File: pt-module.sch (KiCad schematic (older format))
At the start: 6 parts

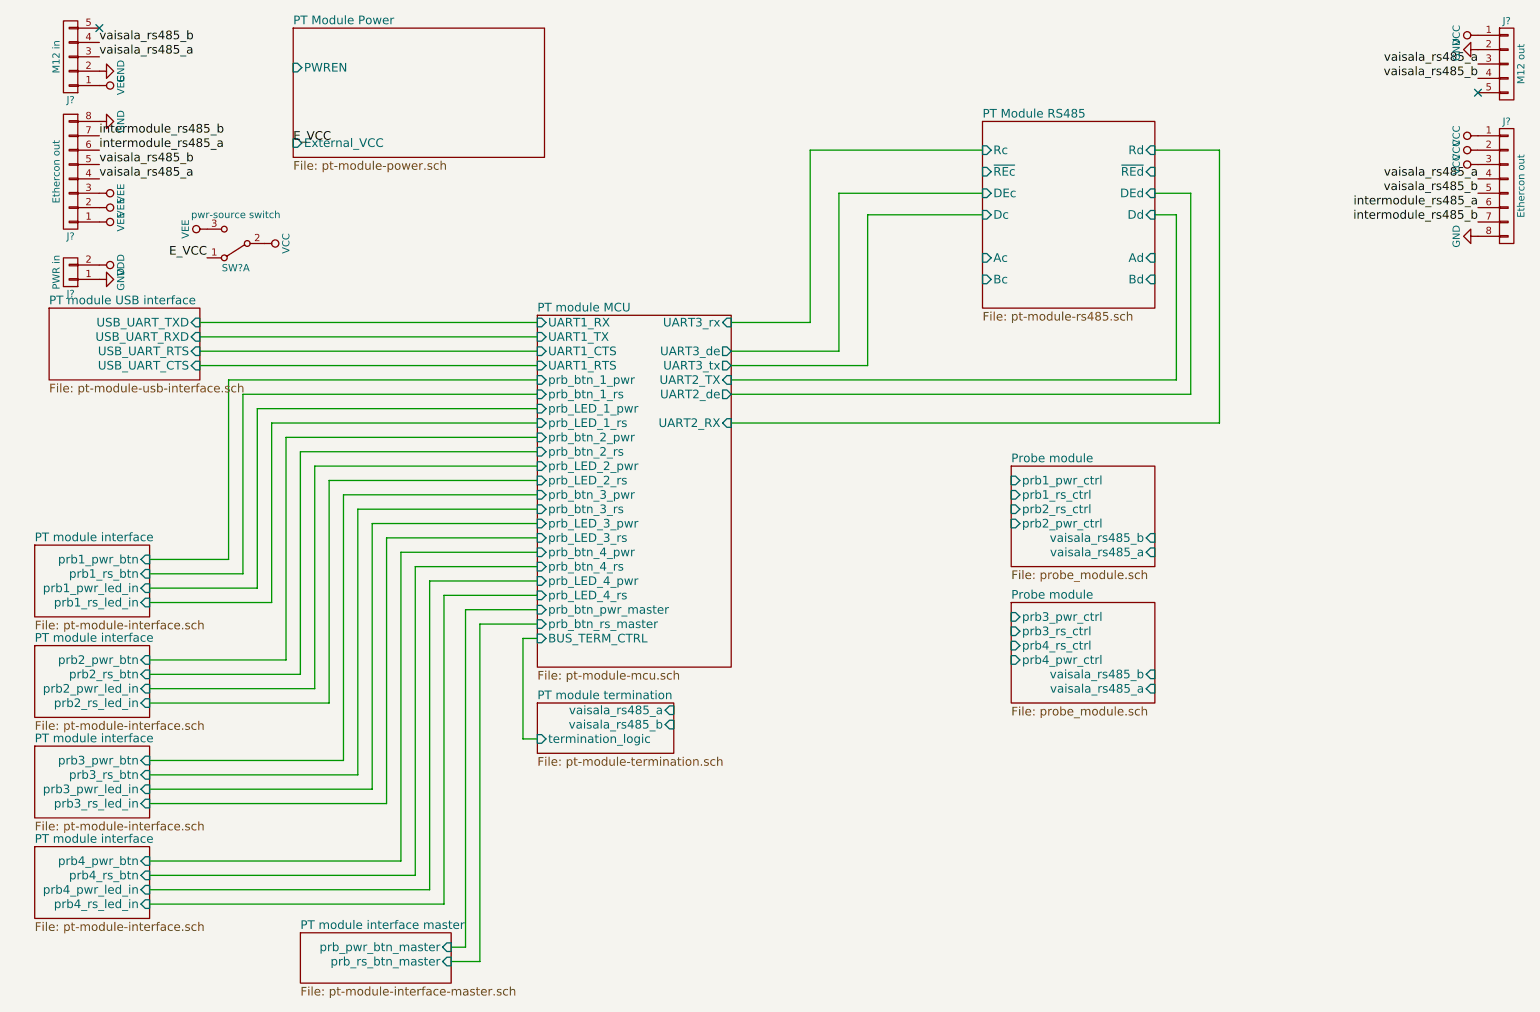
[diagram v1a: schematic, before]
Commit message: Fixed missing components
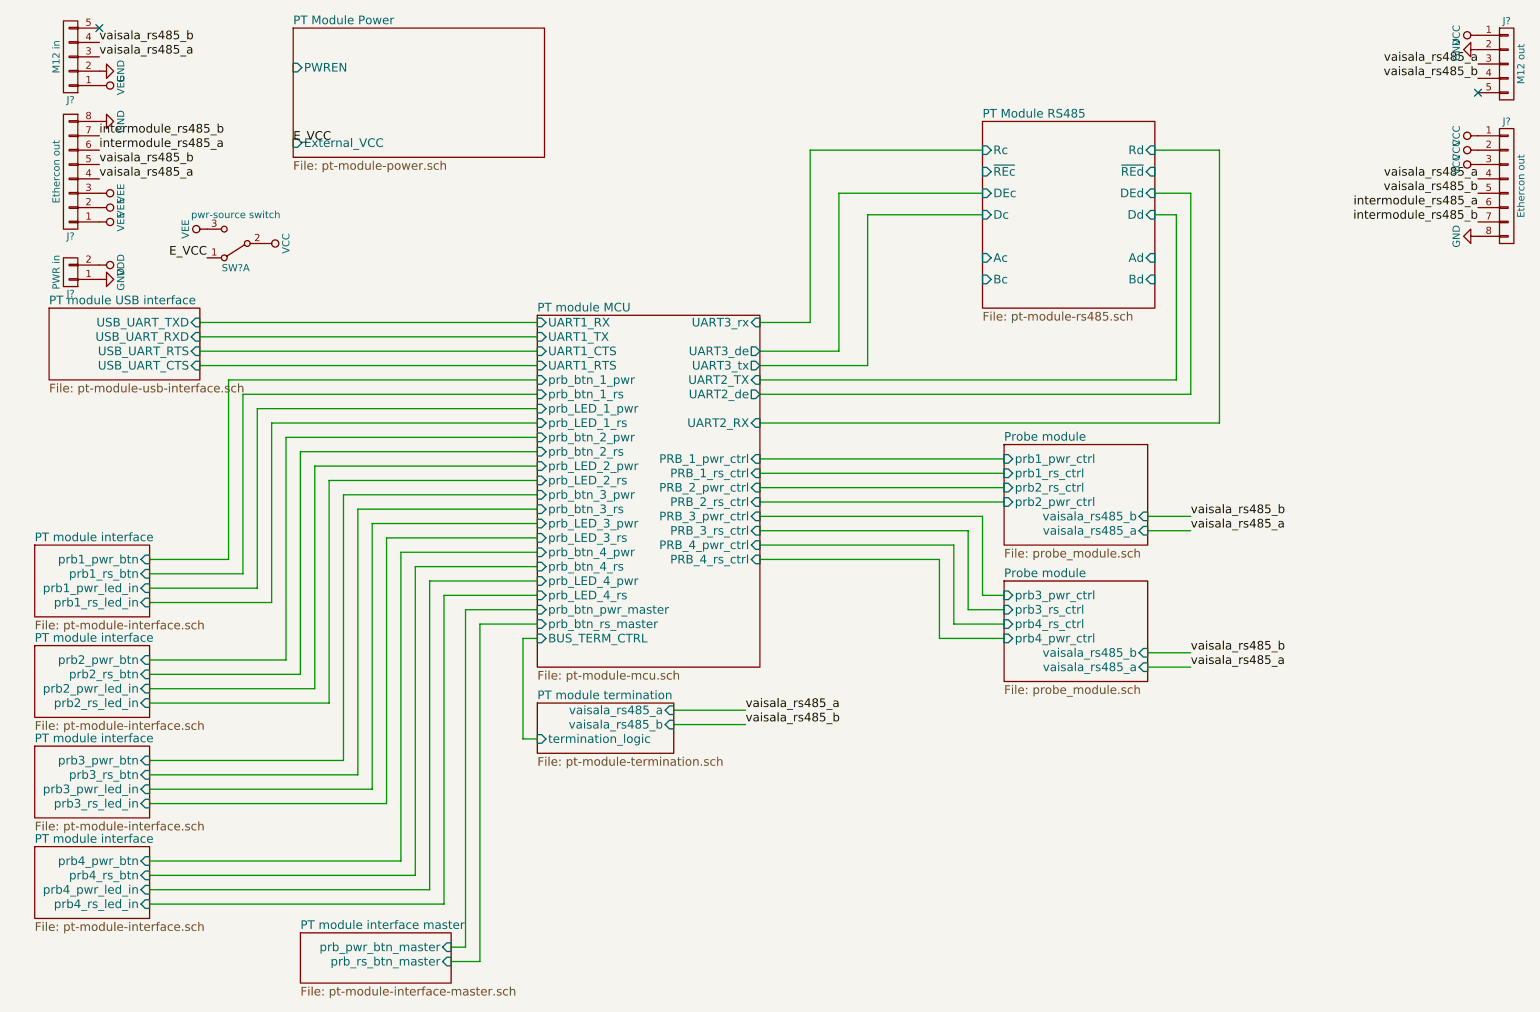
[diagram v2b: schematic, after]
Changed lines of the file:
@@
 LIBS:ftdi
 LIBS:relays
-LIBS:components
 LIBS:pt-module-cache
 EELAYER 25 0
@@
 $EndSheet
 $Sheet
-S 7400 3850 1000 700
+S 7350 3700 1000 700
 U 598183C5
 F0 "Probe module" 60
 F1 "probe_module.sch" 60
-F2 "prb1_pwr_ctrl" I L 7400 3950 60
-F3 "prb1_rs_ctrl" I L 7400 4050 60
-F4 "prb2_rs_ctrl" I L 7400 4150 60
-F5 "prb2_pwr_ctrl" I L 7400 4250 60
-F6 "vaisala_rs485_a" I R 8400 4450 60
-F7 "vaisala_rs485_b" I R 8400 4350 60
+F2 "prb1_pwr_ctrl" I L 7350 3800 60
+F3 "prb1_rs_ctrl" I L 7350 3900 60
+F4 "prb2_rs_ctrl" I L 7350 4000 60
+F5 "prb2_pwr_ctrl" I L 7350 4100 60
+F6 "vaisala_rs485_a" I R 8350 4300 60
+F7 "vaisala_rs485_b" I R 8350 4200 60
 $EndSheet
 $Sheet
@@
 $EndSheet
 $Sheet
-S 4100 2800 1350 2450
+S 4100 2800 1550 2450
 U 5980766A
 F0 "PT module MCU" 60
 F1 "pt-module-mcu.sch" 60
-F2 "UART3_tx" O R 5450 3150 60
-F3 "UART3_rx" I R 5450 2850 60
-F4 "UART3_de" O R 5450 3050 60
+F2 "UART3_tx" O R 5650 3150 60
+F3 "UART3_rx" I R 5650 2850 60
+F4 "UART3_de" O R 5650 3050 60
 F5 "UART1_TX" I L 4100 2950 60
 F6 "UART1_RX" I L 4100 2850 60
 F7 "UART1_CTS" I L 4100 3050 60
 F8 "UART1_RTS" I L 4100 3150 60
-F9 "UART2_RX" I R 5450 3550 60
-F10 "UART2_TX" I R 5450 3250 60
-F11 "UART2_de" O R 5450 3350 60
+F9 "UART2_RX" I R 5650 3550 60
+F10 "UART2_TX" I R 5650 3250 60
+F11 "UART2_de" O R 5650 3350 60
 F12 "BUS_TERM_CTRL" I L 4100 5050 60
 F13 "prb_btn_1_pwr" I L 4100 3250 60
@@
 F29 "prb_btn_pwr_master" I L 4100 4850 60
 F30 "prb_btn_rs_master" I L 4100 4950 60
+F31 "PRB_1_pwr_ctrl" I R 5650 3800 60
+F32 "PRB_1_rs_ctrl" I R 5650 3900 60
+F33 "PRB_2_rs_ctrl" I R 5650 4100 60
+F34 "PRB_2_pwr_ctrl" I R 5650 4000 60
+F35 "PRB_3_pwr_ctrl" I R 5650 4200 60
+F36 "PRB_4_pwr_ctrl" I R 5650 4400 60
+F37 "PRB_3_rs_ctrl" I R 5650 4300 60
+F38 "PRB_4_rs_ctrl" I R 5650 4500 60
 $EndSheet
 $Sheet
@@
 F3 "prb_rs_btn_master" I R 3500 7300 60
 $EndSheet
-Wire Wire Line
-	6200 1950 7200 1950
-Wire Wire Line
-	6000 1650 7200 1650
-Wire Wire Line
-	6400 2100 7200 2100
-Wire Wire Line
-	8400 2100 8550 2100
-Wire Wire Line
-	8650 1950 8400 1950
-Wire Wire Line
-	8850 1650 8400 1650
-Wire Wire Line
-	1750 2850 4100 2850
-Wire Wire Line
-	1750 2950 4100 2950
-Wire Wire Line
-	1750 3050 4100 3050
-Wire Wire Line
-	1750 3150 4100 3150
-Wire Wire Line
-	1950 3250 4100 3250
-Wire Wire Line
-	2050 3350 4100 3350
-Wire Wire Line
-	2150 3450 4100 3450
-Wire Wire Line
-	2250 3550 4100 3550
-Wire Wire Line
-	3450 4750 4100 4750
-Wire Wire Line
-	3350 4650 4100 4650
-Wire Wire Line
-	3150 4450 4100 4450
-Wire Wire Line
-	1400 6200 3050 6200
-Wire Wire Line
-	3050 4350 4100 4350
-Wire Wire Line
-	2950 4250 4100 4250
-Wire Wire Line
-	2950 6100 1400 6100
-Wire Wire Line
-	1400 6000 2850 6000
-Wire Wire Line
-	2850 4150 4100 4150
-Wire Wire Line
-	2750 4050 4100 4050
-Wire Wire Line
-	2750 5900 1400 5900
-Wire Wire Line
-	1400 5500 2650 5500
-Wire Wire Line
-	2650 3950 4100 3950
-Wire Wire Line
-	1400 5400 2550 5400
-Wire Wire Line
-	2550 3850 4100 3850
-Wire Wire Line
-	1400 5300 2450 5300
-Wire Wire Line
-	2450 3750 4100 3750
-Wire Wire Line
-	1400 5200 2350 5200
-Wire Wire Line
-	2350 3650 4100 3650
-Wire Wire Line
-	2250 4800 1400 4800
-Wire Wire Line
-	2150 4700 1400 4700
-Wire Wire Line
-	1400 4600 2050 4600
-Wire Wire Line
-	1950 4500 1400 4500
-Wire Wire Line
-	6000 1650 6000 2850
-Wire Wire Line
-	6000 2850 5450 2850
-Wire Wire Line
-	6200 1950 6200 3050
-Wire Wire Line
-	6200 3050 5450 3050
-Wire Wire Line
-	5450 3150 6400 3150
-Wire Wire Line
-	6400 3150 6400 2100
-Wire Wire Line
-	5450 3250 8550 3250
-Wire Wire Line
-	8550 3250 8550 2100
-Wire Wire Line
-	8650 1950 8650 3350
-Wire Wire Line
-	8650 3350 5450 3350
-Wire Wire Line
-	8850 1650 8850 3550
-Wire Wire Line
-	8850 3550 5450 3550
-Wire Wire Line
-	4100 5050 4000 5050
-Wire Wire Line
-	4000 5050 4000 5750
-Wire Wire Line
-	4000 5750 4100 5750
-Wire Wire Line
-	3700 4950 4100 4950
-Wire Wire Line
-	3600 4850 4100 4850
-Wire Wire Line
-	3050 6200 3050 4350
-Wire Wire Line
-	2950 4250 2950 6100
-Wire Wire Line
-	2850 6000 2850 4150
-Wire Wire Line
-	2750 4050 2750 5900
-Wire Wire Line
-	2650 5500 2650 3950
-Wire Wire Line
-	2550 5400 2550 3850
-Wire Wire Line
-	2450 5300 2450 3750
-Wire Wire Line
-	2350 5200 2350 3650
-Wire Wire Line
-	2250 4800 2250 3550
-Wire Wire Line
-	2150 4700 2150 3450
-Wire Wire Line
-	2050 4600 2050 3350
-Wire Wire Line
-	1950 4500 1950 3250
-Wire Wire Line
-	3150 4450 3150 6600
-Wire Wire Line
-	3150 6600 1400 6600
-Wire Wire Line
-	1400 6700 3250 6700
-Wire Wire Line
-	3250 6700 3250 4550
-Wire Wire Line
-	3250 4550 4100 4550
 $Sheet
 S 600  6500 800  500
@@
 F5 "prb4_rs_led_in" I R 1400 6900 60
 $EndSheet
-Wire Wire Line
-	1400 6800 3350 6800
-Wire Wire Line
-	3350 6800 3350 4650
-Wire Wire Line
-	1400 6900 3450 6900
-Wire Wire Line
-	3450 6900 3450 4750
-Wire Wire Line
-	3500 7200 3600 7200
-Wire Wire Line
-	3600 7200 3600 4850
-Wire Wire Line
-	3500 7300 3700 7300
-Wire Wire Line
-	3700 7300 3700 4950
-$Sheet
-S 7400 4800 1000 700
+$Sheet
+S 7350 4650 1000 700
 U 59933B07
 F0 "Probe module" 60
 F1 "probe_module.sch" 60
-F2 "prb3_pwr_ctrl" I L 7400 4900 60
-F3 "prb3_rs_ctrl" I L 7400 5000 60
-F4 "prb4_rs_ctrl" I L 7400 5100 60
-F5 "prb4_pwr_ctrl" I L 7400 5200 60
-F6 "vaisala_rs485_a" I R 8400 5400 60
-F7 "vaisala_rs485_b" I R 8400 5300 60
-$EndSheet
+F2 "prb3_pwr_ctrl" I L 7350 4750 60
+F3 "prb3_rs_ctrl" I L 7350 4850 60
+F4 "prb4_rs_ctrl" I L 7350 4950 60
+F5 "prb4_pwr_ctrl" I L 7350 5050 60
+F6 "vaisala_rs485_a" I R 8350 5250 60
+F7 "vaisala_rs485_b" I R 8350 5150 60
+$EndSheet
+Text Label 8650 4200 0    60   ~ 0
+vaisala_rs485_b
+Wire Wire Line
+	6000 1650 7200 1650
+Wire Wire Line
+	6400 2100 7200 2100
+Wire Wire Line
+	8400 2100 8550 2100
+Wire Wire Line
+	8650 1950 8400 1950
+Wire Wire Line
+	8850 1650 8400 1650
+Wire Wire Line
+	1750 2850 4100 2850
+Wire Wire Line
+	1750 2950 4100 2950
+Wire Wire Line
+	1750 3050 4100 3050
+Wire Wire Line
+	1750 3150 4100 3150
+Wire Wire Line
+	1950 3250 4100 3250
+Wire Wire Line
+	2050 3350 4100 3350
+Wire Wire Line
+	2150 3450 4100 3450
+Wire Wire Line
+	2250 3550 4100 3550
+Wire Wire Line
+	3450 4750 4100 4750
+Wire Wire Line
+	3350 4650 4100 4650
+Wire Wire Line
+	3150 4450 4100 4450
+Wire Wire Line
+	1400 6200 3050 6200
+Wire Wire Line
+	3050 4350 4100 4350
+Wire Wire Line
+	2950 4250 4100 4250
+Wire Wire Line
+	2950 6100 1400 6100
+Wire Wire Line
+	1400 6000 2850 6000
+Wire Wire Line
+	2850 4150 4100 4150
+Wire Wire Line
+	2750 4050 4100 4050
+Wire Wire Line
+	2750 5900 1400 5900
+Wire Wire Line
+	1400 5500 2650 5500
+Wire Wire Line
+	2650 3950 4100 3950
+Wire Wire Line
+	1400 5400 2550 5400
+Wire Wire Line
+	2550 3850 4100 3850
+Wire Wire Line
+	1400 5300 2450 5300
+Wire Wire Line
+	2450 3750 4100 3750
+Wire Wire Line
+	1400 5200 2350 5200
+Wire Wire Line
+	2350 3650 4100 3650
+Wire Wire Line
+	2250 4800 1400 4800
+Wire Wire Line
+	2150 4700 1400 4700
+Wire Wire Line
+	1400 4600 2050 4600
+Wire Wire Line
+	1950 4500 1400 4500
+Wire Wire Line
+	6000 1650 6000 2850
+Wire Wire Line
+	6200 1950 6200 3050
+Wire Wire Line
+	6400 3150 6400 2100
+Wire Wire Line
+	8550 2100 8550 3250
+Wire Wire Line
+	8650 1950 8650 3350
+Wire Wire Line
+	8850 1650 8850 3550
+Wire Wire Line
+	4100 5050 4000 5050
+Wire Wire Line
+	4000 5050 4000 5750
+Wire Wire Line
+	4000 5750 4100 5750
+Wire Wire Line
+	3700 4950 4100 4950
+Wire Wire Line
+	3600 4850 4100 4850
+Wire Wire Line
+	3050 6200 3050 4350
+Wire Wire Line
+	2950 4250 2950 6100
+Wire Wire Line
+	2850 6000 2850 4150
+Wire Wire Line
+	2750 4050 2750 5900
+Wire Wire Line
+	2650 5500 2650 3950
+Wire Wire Line
+	2550 5400 2550 3850
+Wire Wire Line
+	2450 5300 2450 3750
+Wire Wire Line
+	2350 5200 2350 3650
+Wire Wire Line
+	2250 4800 2250 3550
+Wire Wire Line
+	2150 4700 2150 3450
+Wire Wire Line
+	2050 4600 2050 3350
+Wire Wire Line
+	1950 4500 1950 3250
+Wire Wire Line
+	3150 4450 3150 6600
+Wire Wire Line
+	3150 6600 1400 6600
+Wire Wire Line
+	1400 6700 3250 6700
+Wire Wire Line
+	3250 6700 3250 4550
+Wire Wire Line
+	3250 4550 4100 4550
+Wire Wire Line
+	1400 6800 3350 6800
+Wire Wire Line
+	3350 6800 3350 4650
+Wire Wire Line
+	1400 6900 3450 6900
+Wire Wire Line
+	3450 6900 3450 4750
+Wire Wire Line
+	3500 7200 3600 7200
+Wire Wire Line
+	3600 7200 3600 4850
+Wire Wire Line
+	3500 7300 3700 7300
+Wire Wire Line
+	3700 7300 3700 4950
+Wire Wire Line
+	6000 2850 5650 2850
+Wire Wire Line
+	7350 3800 5650 3800
+Wire Wire Line
+	7350 3900 5650 3900
+Wire Wire Line
+	5650 4000 7350 4000
+Wire Wire Line
+	7350 4100 5650 4100
+Wire Wire Line
+	7350 5050 6900 5050
+Wire Wire Line
+	6900 5050 6900 4500
+Wire Wire Line
+	6900 4500 5650 4500
+Wire Wire Line
+	7350 4950 7000 4950
+Wire Wire Line
+	7000 4950 7000 4400
+Wire Wire Line
+	7000 4400 5650 4400
+Wire Wire Line
+	7350 4850 7100 4850
+Wire Wire Line
+	7100 4850 7100 4300
+Wire Wire Line
+	7100 4300 5650 4300
+Wire Wire Line
+	7350 4750 7200 4750
+Wire Wire Line
+	7200 4750 7200 4200
+Wire Wire Line
+	7200 4200 5650 4200
+Wire Wire Line
+	6200 1950 7200 1950
+Wire Wire Line
+	6200 3050 5650 3050
+Wire Wire Line
+	6400 3150 5650 3150
+Wire Wire Line
+	8550 3250 5650 3250
+Wire Wire Line
+	8650 3350 5650 3350
+Wire Wire Line
+	8850 3550 5650 3550
+Wire Wire Line
+	8650 4200 8350 4200
+Text Label 8650 5150 0    60   ~ 0
+vaisala_rs485_b
+Wire Wire Line
+	8650 5150 8350 5150
+Text Label 8650 4300 0    60   ~ 0
+vaisala_rs485_a
+Text Label 8650 5250 0    60   ~ 0
+vaisala_rs485_a
+Wire Wire Line
+	8650 4300 8350 4300
+Wire Wire Line
+	8350 5250 8650 5250
+Text Label 5550 5650 0    60   ~ 0
+vaisala_rs485_b
+Text Label 5550 5550 0    60   ~ 0
+vaisala_rs485_a
+Wire Wire Line
+	5550 5550 5050 5550
+Wire Wire Line
+	5050 5650 5550 5650
 $EndSCHEMATC

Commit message: Connected EVERYTHING. Ran ERC. There are still some power errors.
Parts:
- gave numbers to parts that had none: 6
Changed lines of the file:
@@
 LIBS:ftdi
 LIBS:relays
+LIBS:microchip_dspic33dsc
+LIBS:microchip_pic10mcu
+LIBS:microchip_pic12mcu
+LIBS:microchip_pic16mcu
+LIBS:microchip_pic18mcu
+LIBS:microchip_pic24mcu
+LIBS:microchip_pic32mcu
 LIBS:pt-module-cache
 EELAYER 25 0
@@
 $EndSheet
 $Comp
-L CONN_01X05 J?
+L CONN_01X05 J4
 U 1 1 59820FE7
 P 10850 1050
-F 0 "J?" H 10850 1350 50  0000 C CNN
+F 0 "J4" H 10850 1350 50  0000 C CNN
 F 1 "M12 out" V 10950 1050 50  0000 C CNN
 F 2 "" H 10850 1050 50  0001 C CNN
@@
 NoConn ~ 10650 1250
 $Comp
-L CONN_01X08 J?
+L CONN_01X08 J5
 U 1 1 59829448
 P 10850 1900
-F 0 "J?" H 10850 2350 50  0000 C CNN
+F 0 "J5" H 10850 2350 50  0000 C CNN
 F 1 "Ethercon out" V 10950 1900 50  0000 C CNN
 F 2 "" H 10850 1900 50  0001 C CNN
@@
 $EndComp
 $Comp
-L CONN_01X05 J?
+L CONN_01X05 J1
 U 1 1 5982A52D
 P 850 1000
-F 0 "J?" H 850 1300 50  0000 C CNN
+F 0 "J1" H 850 1300 50  0000 C CNN
 F 1 "M12 in" V 950 1000 50  0000 C CNN
 F 2 "" H 850 1000 50  0001 C CNN
@@
 $EndComp
 $Comp
-L CONN_01X08 J?
+L CONN_01X08 J2
 U 1 1 59840D9B
 P 850 1800
-F 0 "J?" H 850 2250 50  0000 C CNN
+F 0 "J2" H 850 2250 50  0000 C CNN
 F 1 "Ethercon out" V 950 1800 50  0000 C CNN
 F 2 "" H 850 1800 50  0001 C CNN
@@
 intermodule_rs485_b
 $Comp
-L CONN_01X02 J?
+L CONN_01X02 J3
 U 1 1 5984EE28
 P 850 2500
-F 0 "J?" H 850 2650 50  0000 C CNN
+F 0 "J3" H 850 2650 50  0000 C CNN
 F 1 "PWR in" V 950 2500 50  0000 C CNN
 F 2 "" H 850 2500 50  0001 C CNN
@@
 $EndComp
 $Comp
-L SW_DPDT_x2 SW?
+L SW_DPDT_x2 SW1
 U 1 1 5985369A
 P 2000 2300
-F 0 "SW?" H 2000 2470 50  0000 C CNN
+F 0 "SW1" H 2000 2470 50  0000 C CNN
 F 1 "pwr-source switch" H 2000 2100 50  0000 C CNN
 F 2 "" H 2000 2300 50  0001 C CNN
@@
 S 600  5100 800  500
 U 598B38EB
-F0 "PT module interface" 60
-F1 "pt-module-interface.sch" 60
+F0 "PT module interface 2" 60
+F1 "pt-module-interface2.sch" 60
 F2 "prb2_pwr_btn" I R 1400 5200 60
 F3 "prb2_pwr_led_in" I R 1400 5400 60
@@
 S 600  5800 800  500
 U 598B3EA9
-F0 "PT module interface" 60
-F1 "pt-module-interface.sch" 60
+F0 "PT module interface 3" 60
+F1 "pt-module-interface3.sch" 60
 F2 "prb3_pwr_btn" I R 1400 5900 60
 F3 "prb3_pwr_led_in" I R 1400 6100 60
@@
 S 600  6500 800  500
 U 598B41A3
-F0 "PT module interface" 60
-F1 "pt-module-interface.sch" 60
+F0 "PT module interface 4" 60
+F1 "pt-module-interface4.sch" 60
 F2 "prb4_pwr_btn" I R 1400 6600 60
 F3 "prb4_pwr_led_in" I R 1400 6800 60
@@
 S 7350 4650 1000 700
 U 59933B07
-F0 "Probe module" 60
-F1 "probe_module.sch" 60
+F0 "Probe module 2" 60
+F1 "probe_module2.sch" 60
 F2 "prb3_pwr_ctrl" I L 7350 4750 60
 F3 "prb3_rs_ctrl" I L 7350 4850 60
@@
 Wire Wire Line
 	5050 5650 5550 5650
+Text Label 9000 2400 0    60   ~ 0
+vaisala_rs485_a
+Text Label 9000 2550 0    60   ~ 0
+vaisala_rs485_b
+Wire Wire Line
+	9000 2400 8400 2400
+Wire Wire Line
+	9000 2550 8400 2550
+Text Label 6850 3100 0    60   ~ 0
+intermodule_rs485_a
+Text Label 6850 3000 0    60   ~ 0
+intermodule_rs485_b
+Wire Wire Line
+	7200 2550 6800 2550
+Wire Wire Line
+	6800 2550 6800 3000
+Wire Wire Line
+	6800 3000 6850 3000
+Wire Wire Line
+	6850 3100 6700 3100
+Wire Wire Line
+	6700 3100 6700 2400
+Wire Wire Line
+	6700 2400 7200 2400
+Wire Wire Line
+	7200 1800 7000 1800
+Wire Wire Line
+	7000 1800 7000 1950
+Connection ~ 7000 1950
+Wire Wire Line
+	8400 1800 8600 1800
+Wire Wire Line
+	8600 1800 8600 1950
+Connection ~ 8600 1950
 $EndSCHEMATC

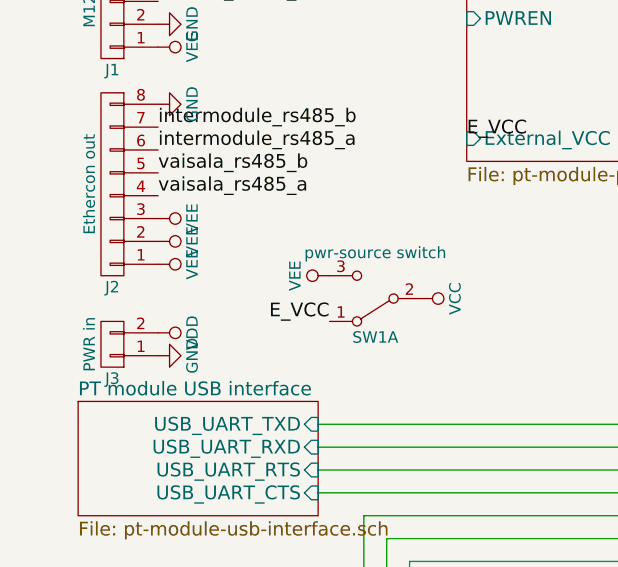
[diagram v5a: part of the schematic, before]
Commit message: Only 1 error in ERC check. It's in PWREN.
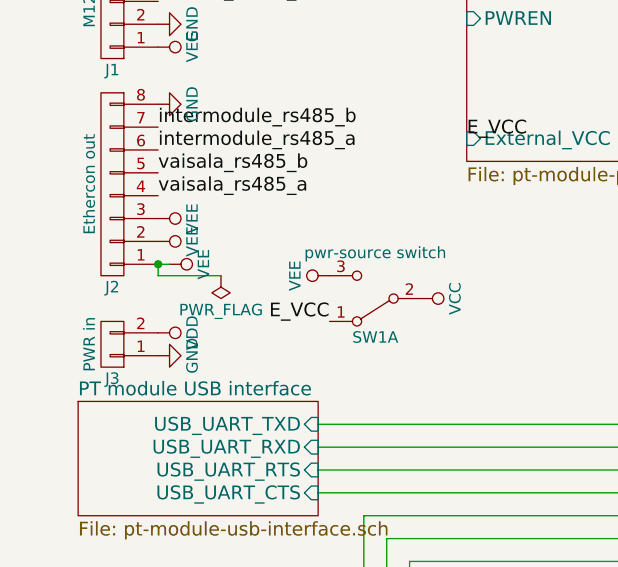
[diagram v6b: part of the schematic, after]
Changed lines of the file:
@@
 L VEE #PWR013
 U 1 1 5985D494
-P 1050 2150
-F 0 "#PWR013" H 1050 2000 50  0001 C CNN
-F 1 "VEE" H 1050 2300 50  0000 C CNN
-F 2 "" H 1050 2150 50  0001 C CNN
-F 3 "" H 1050 2150 50  0001 C CNN
-	1    1050 2150
+P 1100 2150
+F 0 "#PWR013" H 1100 2000 50  0001 C CNN
+F 1 "VEE" H 1100 2300 50  0000 C CNN
+F 2 "" H 1100 2150 50  0001 C CNN
+F 3 "" H 1100 2150 50  0001 C CNN
+	1    1100 2150
 	0    1    1    0
 $EndComp
@@
 	8600 1800 8600 1950
 Connection ~ 8600 1950
+$Comp
+L PWR_FLAG #FLG017
+U 1 1 5996610E
+P 1325 2200
+F 0 "#FLG017" H 1325 2275 50  0001 C CNN
+F 1 "PWR_FLAG" H 1325 2350 50  0000 C CNN
+F 2 "" H 1325 2200 50  0001 C CNN
+F 3 "" H 1325 2200 50  0001 C CNN
+	1    1325 2200
+	-1   0    0    1
+$EndComp
+Wire Wire Line
+	1325 2200 1050 2200
+Wire Wire Line
+	1050 2200 1050 2150
+Wire Wire Line
+	1050 2150 1100 2150
+Connection ~ 1050 2150
 $EndSCHEMATC
